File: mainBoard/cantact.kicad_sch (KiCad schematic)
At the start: 35 parts, among them J1 Cantact, P2 SWD, P4 USB_C_Plug_USB2.0, U1 STM32F042C6T6, U3 MCP2551-I/SN, U4 XC6220B331MR-G, Y1 16 Mhz

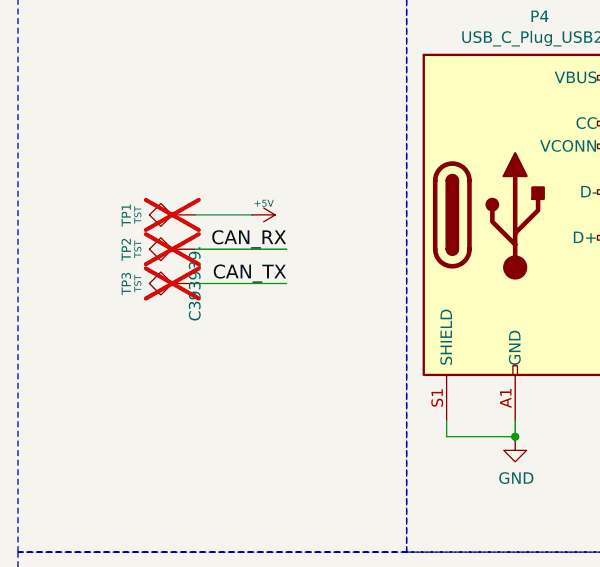
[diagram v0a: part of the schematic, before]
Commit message: feat(Hw):Update_Labels_And_BOM
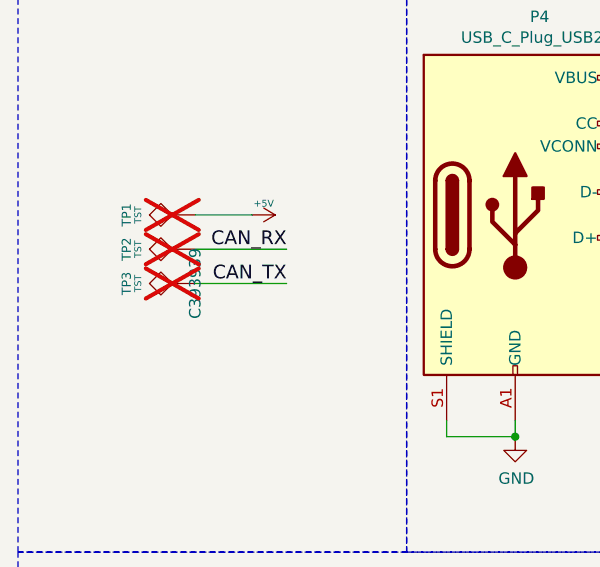
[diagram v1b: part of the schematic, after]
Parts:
- R1: LCSC# C217366 -> C2907179
- R10, R11: LCSC# C191782 -> C227511
- TP3: LCSC# C393939. -> C393939
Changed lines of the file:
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@@
 			)
 		)
-		(property "LCSC#" "C217366"
+		(property "LCSC#" "C2907179"
 			(at 77.47 161.29 0)
 			(effects
@@
 			)
 		)
-		(property "LCSC#" "C393939."
+		(property "LCSC#" "C393939"
 			(at 31.75 52.07 0)
 			(effects
@@
 			)
 		)
-		(property "LCSC#" "C191782"
+		(property "LCSC#" "C227511"
 			(at 86.868 34.29 0)
 			(effects
@@
 			)
 		)
-		(property "LCSC#" "C191782"
+		(property "LCSC#" "C227511"
 			(at 86.868 36.83 0)
 			(effects

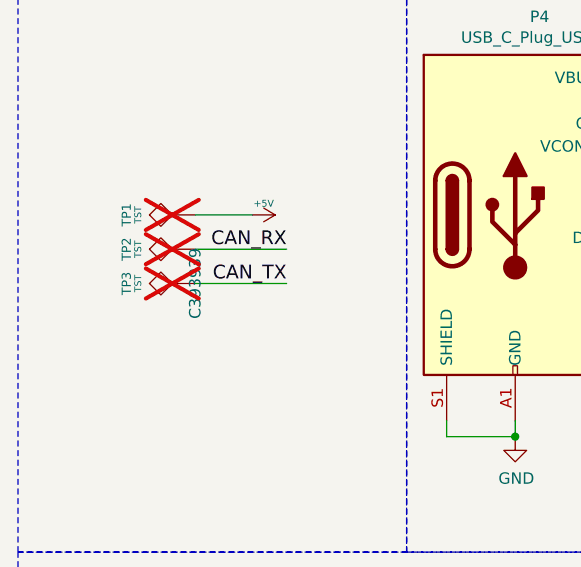
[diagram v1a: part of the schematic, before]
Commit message: fix: change footprint
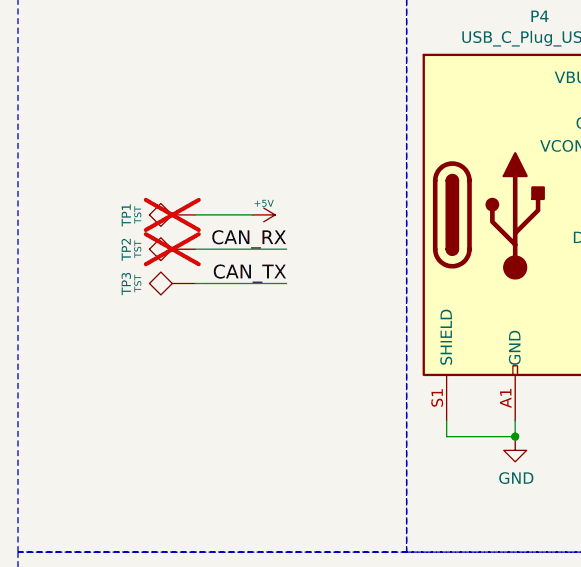
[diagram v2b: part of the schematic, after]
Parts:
- JP1: LCSC# C7501580 -> (none)
- P2: LCSC# C7501583 -> (none)
- P4: LCSC# C393939 -> (none)
- TP3: LCSC# C393939 -> (none); now fitted
- U3: footprint SMD_Packages:SOIC-8-N -> Package_SO:SOIC-8_3.9x4.9mm_P1.27mm
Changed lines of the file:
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@@
 			)
 		)
-		(property "Footprint" "SMD_Packages:SOIC-8-N"
+		(property "Footprint" "Package_SO:SOIC-8_3.9x4.9mm_P1.27mm"
 			(at 203.2 49.53 0)
 			(effects
@@
 			)
 		)
-		(property "LCSC#" "C7501583"
+		(property "LCSC#" ""
 			(at 250.19 104.14 0)
 			(effects
@@
 			)
 		)
-		(property "LCSC#" "C7501580"
+		(property "LCSC#" ""
 			(at 68.072 147.828 0)
 			(effects
@@
 		(in_bom yes)
 		(on_board yes)
-		(dnp yes)
+		(dnp no)
 		(property "Reference" "TP3"
 			(at 24.13 52.07 0)
@@
 			)
 		)
-		(property "LCSC#" "C393939"
+		(property "LCSC#" ""
 			(at 31.75 52.07 0)
 			(effects
@@
 			)
 		)
-		(property "LCSC#" "C393939"
+		(property "LCSC#" ""
 			(at 67.31 44.45 0)
 			(effects
